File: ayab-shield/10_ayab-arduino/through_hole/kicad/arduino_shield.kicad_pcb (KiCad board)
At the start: 2 copper layers, 72 x 54.6 mm, 29 parts, among them IC3 MCP2300X/P, IC4 MCP2300X/P, X1 NEB1R

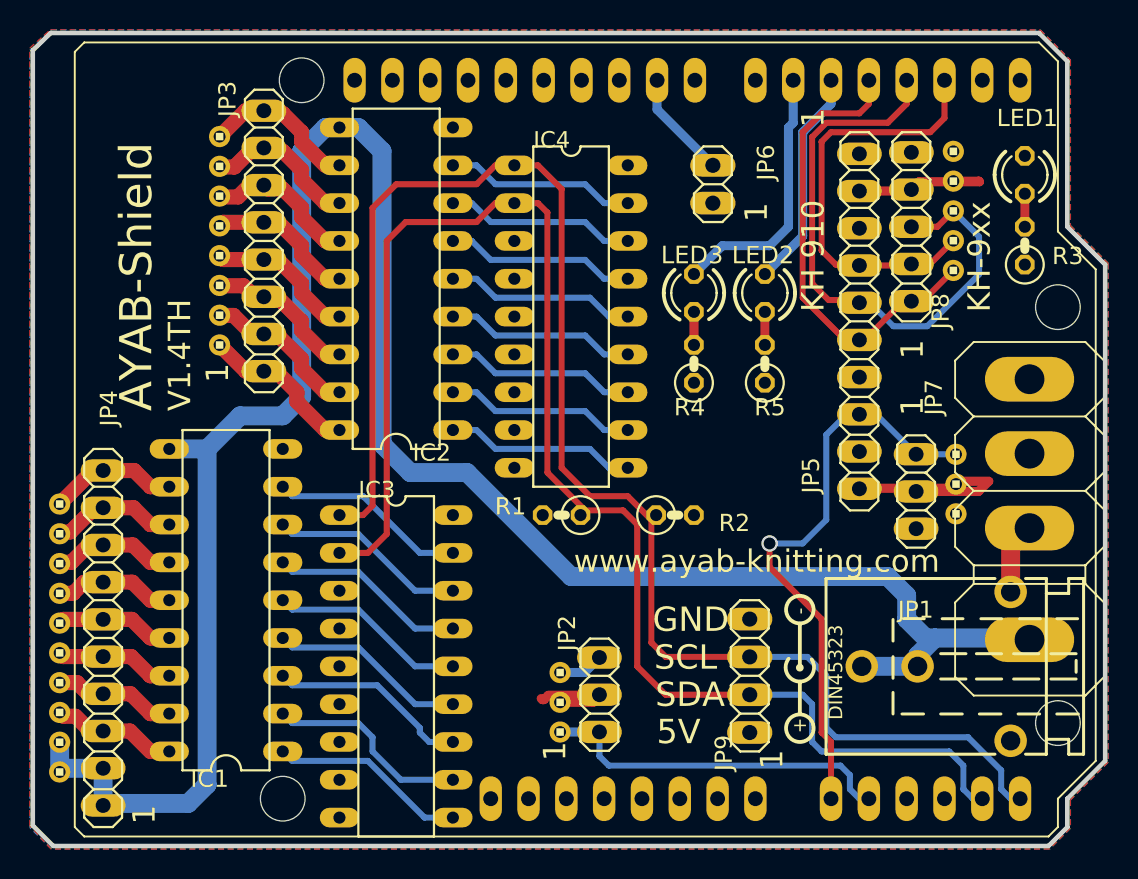
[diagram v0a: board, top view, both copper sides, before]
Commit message: Update Kicad import from Eagle with a schematic and general cleanup. Now features: * A linked schematic matching the Eagle one except cosmetic or Kicad specific requirements (e.g., power flags). * References have been hidden and labels placed to match the Eagle ones, which are incompatible with Kicad. * Cosmetic changes in schematic and layout to account for font, etc differences. * Version updated to "1.4TH Rev A" to make it clear it's a new variant--though should be functionally the same.
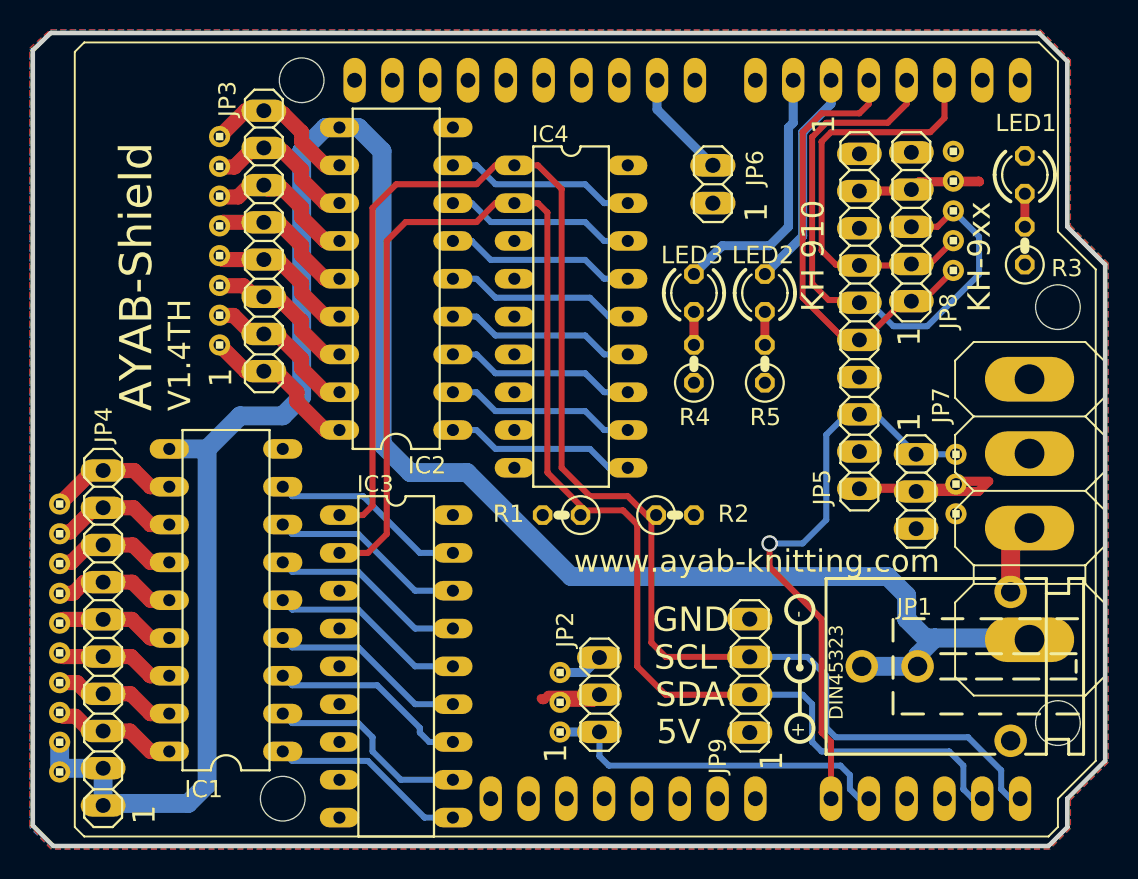
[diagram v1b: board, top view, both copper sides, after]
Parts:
- removed U$2: V1.3TH, arduino_shield:A4L-LOC
- IC1, IC2: value (none) -> ULN2803A
- JP2, JP7: value (none) -> PINHD-1X3
- JP3: value (none) -> PINHD-1X8
- JP4, JP5: value (none) -> PINHD-1X10
- JP6: value (none) -> PINHD-1X2
- JP8: value (none) -> PINHD-1X5
- JP9: value (none) -> PINHD-1X4
- LED1, LED2, LED3: value (none) -> LED3MM
- R1, R2, R3, R4, R5: value (none) -> R-EU_0207/2V
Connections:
- net ENC0PINA renamed /ENC0PINA
- net ENC0PINB renamed /ENC0PINB
- net ENC0PINC renamed /ENC0PINC
- net EOL0L renamed /EOL0L
- net EOL0R renamed /EOL0R
- net RESET renamed /RESET
- net SCL renamed /SCL
- net SDA renamed /SDA
- ARD1 pad 0: (no net) -> unconnected-(ARD1-Pad0)
- ARD1 pad 1: (no net) -> unconnected-(ARD1-Pad1)
- ARD1 pad 10: (no net) -> unconnected-(ARD1-Pad10)
- ARD1 pad 11: (no net) -> unconnected-(ARD1-Pad11)
- ARD1 pad 12: (no net) -> unconnected-(ARD1-Pad12)
- ARD1 pad 13: (no net) -> unconnected-(ARD1-Pad13)
- ARD1 pad 7: (no net) -> unconnected-(ARD1-Pad7)
- ARD1 pad 8: (no net) -> unconnected-(ARD1-Pad8)
- ARD1 pad AIN2: (no net) -> unconnected-(ARD1-PadAIN2)
- ARD1 pad AIN3: (no net) -> unconnected-(ARD1-PadAIN3)
- ARD1 pad SCL: (no net) -> unconnected-(ARD1-PadSCL)
- ARD1 pad SDA: (no net) -> unconnected-(ARD1-PadSDA)
- IC3 pad 8: (no net) -> unconnected-(IC3-Pad8)
- IC4 pad 8: (no net) -> unconnected-(IC4-Pad8)
- JP5 pad 3: (no net) -> unconnected-(JP5-Pad3)
- X1 pad 1@2: (no net) -> unconnected-(X1-Pad1@2)

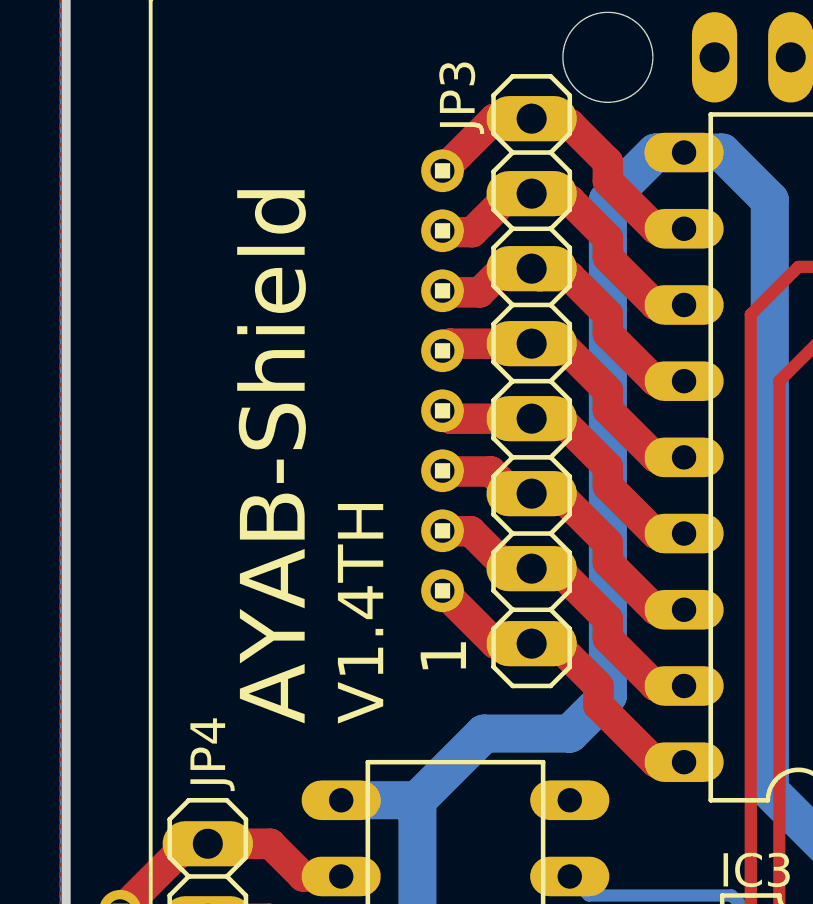
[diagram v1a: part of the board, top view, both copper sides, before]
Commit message: Update revision in PCB silkscreen and regenerate gerbers
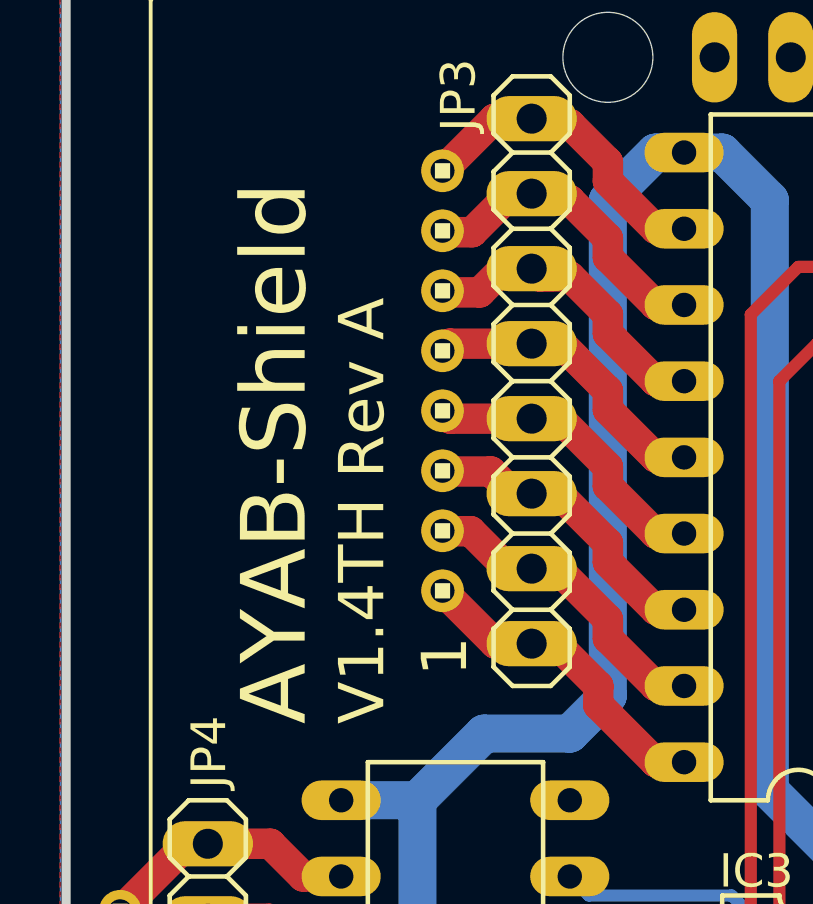
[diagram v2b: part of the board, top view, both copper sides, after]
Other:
- board text added: "V1.4TH Rev A"
- board text removed: "V1.4TH"
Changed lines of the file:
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@@
   )
   (paper "A4")
+  (title_block
+    (title "AYAB-Shield")
+    (date "2024-08-12")
+    (rev "1.4TH Rev A")
+    (company "AYAB Project")
+    (comment 1 "Converted from Eagle format (v1.4TH) with only cosmetic changes")
+  )
   (layers
     (0 "F.Cu" signal)
@@
       (outputformat 1)
       (mirror false)
-      (drillshape 1)
+      (drillshape 0)
       (scaleselection 1)
-      (outputdirectory "")
+      (outputdirectory "../gerber/")
     )
   )
@@
     (effects (font (size 2.159 2.159) (thickness 0.381)) (justify left bottom))
   )
-  (gr_text "V1.4TH" (at 123.2408 103.0986 90) (layer "F.SilkS")
+  (gr_text "V1.4TH Rev A" (at 123.2408 103.0986 90) (layer "F.SilkS")
     (effects (font (size 1.5113 1.5113) (thickness 0.2667)) (justify left bottom))
   )
